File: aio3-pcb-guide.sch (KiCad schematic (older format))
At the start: 16 parts

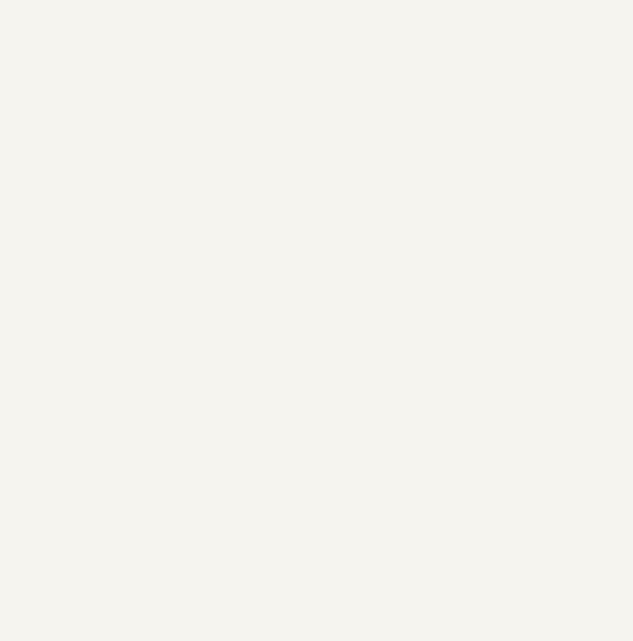
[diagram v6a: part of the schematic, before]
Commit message: [schema](switch): add switch matrix
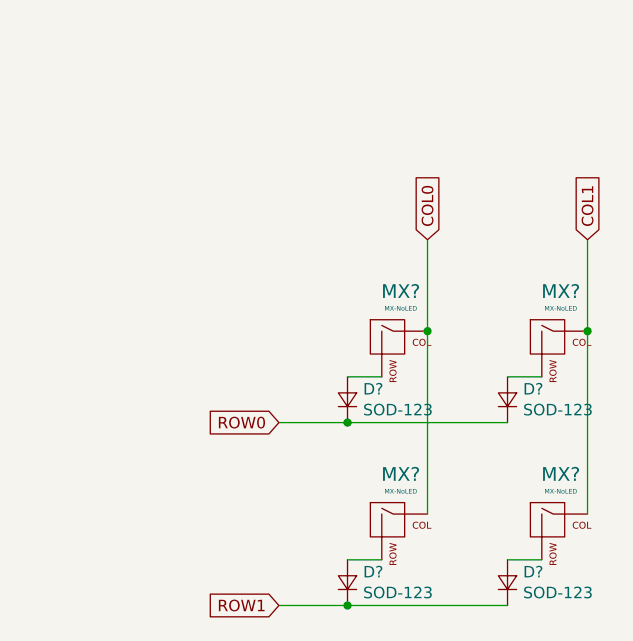
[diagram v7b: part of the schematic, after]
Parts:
- added D? (x4): SOD-123, symbol Device:D_Small
- added MX? (x4): MX-NoLED, symbol MX_Alps_Hybrid:MX-NoLED
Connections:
- new net: D?.2 (A), MX?.2 (ROW) (x4)
- new net COL0: MX?.1 (COL), MX?.1 (COL)
- new net COL1: MX?.1 (COL), MX?.1 (COL)
- new net ROW0: D?.1 (K), D?.1 (K)
- new net ROW1: D?.1 (K), D?.1 (K)
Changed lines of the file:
@@
 Wire Wire Line
 	6200 1950 6100 1950
+$Comp
+L MX_Alps_Hybrid:MX-NoLED MX?
+U 1 1 62009EA0
+P 8250 4250
+F 0 "MX?" H 8283 4473 60  0000 C CNN
+F 1 "MX-NoLED" H 8283 4399 20  0000 C CNN
+F 2 "" H 7625 4225 60  0001 C CNN
+F 3 "" H 7625 4225 60  0001 C CNN
+	1    8250 4250
+	1    0    0    -1
+$EndComp
+$Comp
+L Device:D_Small D?
+U 1 1 6200AA67
+P 8050 4500
+F 0 "D?" V 8096 4432 50  0000 R CNN
+F 1 "SOD-123" V 8005 4432 50  0000 R CNN
+F 2 "" V 8050 4500 50  0001 C CNN
+F 3 "~" V 8050 4500 50  0001 C CNN
+	1    8050 4500
+	0    -1   -1   0
+$EndComp
+Wire Wire Line
+	8050 4400 8200 4400
+$Comp
+L MX_Alps_Hybrid:MX-NoLED MX?
+U 1 1 62019D30
+P 8950 4250
+F 0 "MX?" H 8983 4473 60  0000 C CNN
+F 1 "MX-NoLED" H 8983 4399 20  0000 C CNN
+F 2 "" H 8325 4225 60  0001 C CNN
+F 3 "" H 8325 4225 60  0001 C CNN
+	1    8950 4250
+	1    0    0    -1
+$EndComp
+$Comp
+L Device:D_Small D?
+U 1 1 6201B32F
+P 8750 4500
+F 0 "D?" V 8796 4432 50  0000 R CNN
+F 1 "SOD-123" V 8705 4432 50  0000 R CNN
+F 2 "" V 8750 4500 50  0001 C CNN
+F 3 "~" V 8750 4500 50  0001 C CNN
+	1    8750 4500
+	0    -1   -1   0
+$EndComp
+Wire Wire Line
+	8750 4400 8900 4400
+$Comp
+L MX_Alps_Hybrid:MX-NoLED MX?
+U 1 1 6201CAE2
+P 8950 5050
+F 0 "MX?" H 8983 5273 60  0000 C CNN
+F 1 "MX-NoLED" H 8983 5199 20  0000 C CNN
+F 2 "" H 8325 5025 60  0001 C CNN
+F 3 "" H 8325 5025 60  0001 C CNN
+	1    8950 5050
+	1    0    0    -1
+$EndComp
+$Comp
+L Device:D_Small D?
+U 1 1 6201D0F6
+P 8750 5300
+F 0 "D?" V 8796 5232 50  0000 R CNN
+F 1 "SOD-123" V 8705 5232 50  0000 R CNN
+F 2 "" V 8750 5300 50  0001 C CNN
+F 3 "~" V 8750 5300 50  0001 C CNN
+	1    8750 5300
+	0    -1   -1   0
+$EndComp
+Wire Wire Line
+	8750 5200 8900 5200
+$Comp
+L MX_Alps_Hybrid:MX-NoLED MX?
+U 1 1 6201F1A6
+P 8250 5050
+F 0 "MX?" H 8283 5273 60  0000 C CNN
+F 1 "MX-NoLED" H 8283 5199 20  0000 C CNN
+F 2 "" H 7625 5025 60  0001 C CNN
+F 3 "" H 7625 5025 60  0001 C CNN
+	1    8250 5050
+	1    0    0    -1
+$EndComp
+$Comp
+L Device:D_Small D?
+U 1 1 6201F7BA
+P 8050 5300
+F 0 "D?" V 8096 5232 50  0000 R CNN
+F 1 "SOD-123" V 8005 5232 50  0000 R CNN
+F 2 "" V 8050 5300 50  0001 C CNN
+F 3 "~" V 8050 5300 50  0001 C CNN
+	1    8050 5300
+	0    -1   -1   0
+$EndComp
+Wire Wire Line
+	8050 5200 8200 5200
+Wire Wire Line
+	8400 5000 8400 4200
+Wire Wire Line
+	8400 4200 8400 3800
+Connection ~ 8400 4200
+Wire Wire Line
+	9100 5000 9100 4200
+Connection ~ 9100 4200
+Wire Wire Line
+	9100 4200 9100 3800
+Wire Wire Line
+	8750 4600 8050 4600
+Connection ~ 8050 4600
+Wire Wire Line
+	8050 4600 7750 4600
+Wire Wire Line
+	8750 5400 8050 5400
+Connection ~ 8050 5400
+Wire Wire Line
+	8050 5400 7750 5400
+Text GLabel 7750 4600 0    50   Input ~ 0
+ROW0
+Text GLabel 7750 5400 0    50   Input ~ 0
+ROW1
+Text GLabel 8400 3800 1    50   Input ~ 0
+COL0
+Text GLabel 9100 3800 1    50   Input ~ 0
+COL1
 $EndSCHEMATC

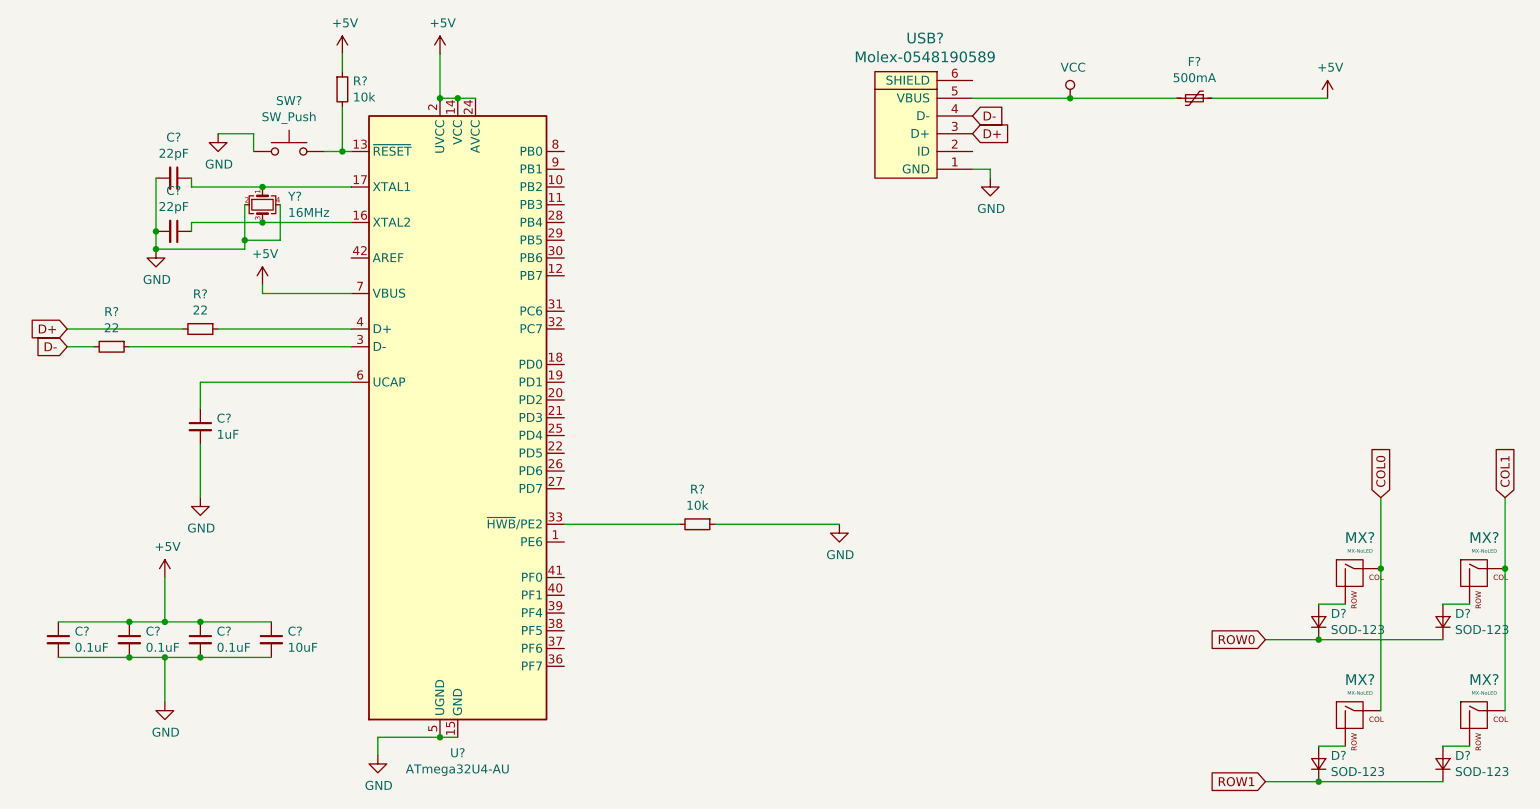
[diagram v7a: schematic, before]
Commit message: [schema]: assign footprints
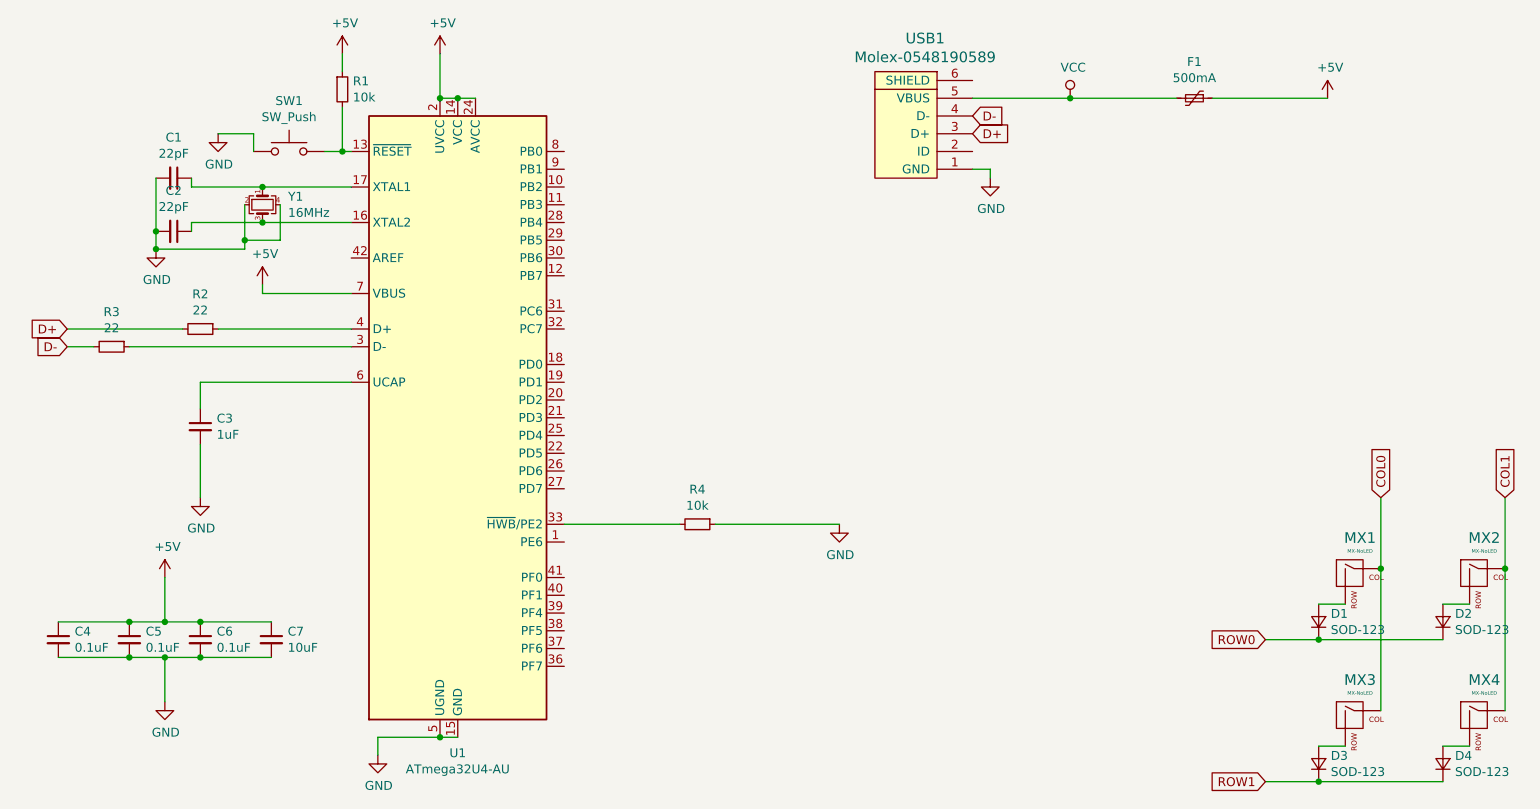
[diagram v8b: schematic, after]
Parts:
- C1, C2, C3, C4, C5, C6, C7: renamed from C?; footprint (none) -> Capacitor_SMD:C_0805_2012Metric
- D1, D2, D3, D4: renamed from D?; footprint (none) -> Diode_SMD:D_SOD-123
- F1: renamed from F?; footprint (none) -> Fuse:Fuse_1206_3216Metric
- MX1, MX2, MX3, MX4: renamed from MX?; footprint (none) -> MX_Alps_Hybrid:MX-1U
- R1, R2, R3, R4: renamed from R?; footprint (none) -> Resistor_SMD:R_0805_2012Metric
- SW1: renamed from SW?; footprint (none) -> random-keyboard-parts:SKQG-1155865
- USB1: renamed from USB?; footprint (none) -> random-keyboard-parts:Molex-0548190589
- Y1: renamed from Y?; footprint (none) -> Crystal:Crystal_SMD_3225-4Pin_3.2x2.5mm
- gave numbers to parts that had none: 1
